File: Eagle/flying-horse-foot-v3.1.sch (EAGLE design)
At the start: 25 parts, among them J2 SPI6, U1 8U2-AU, Y2 16MHz

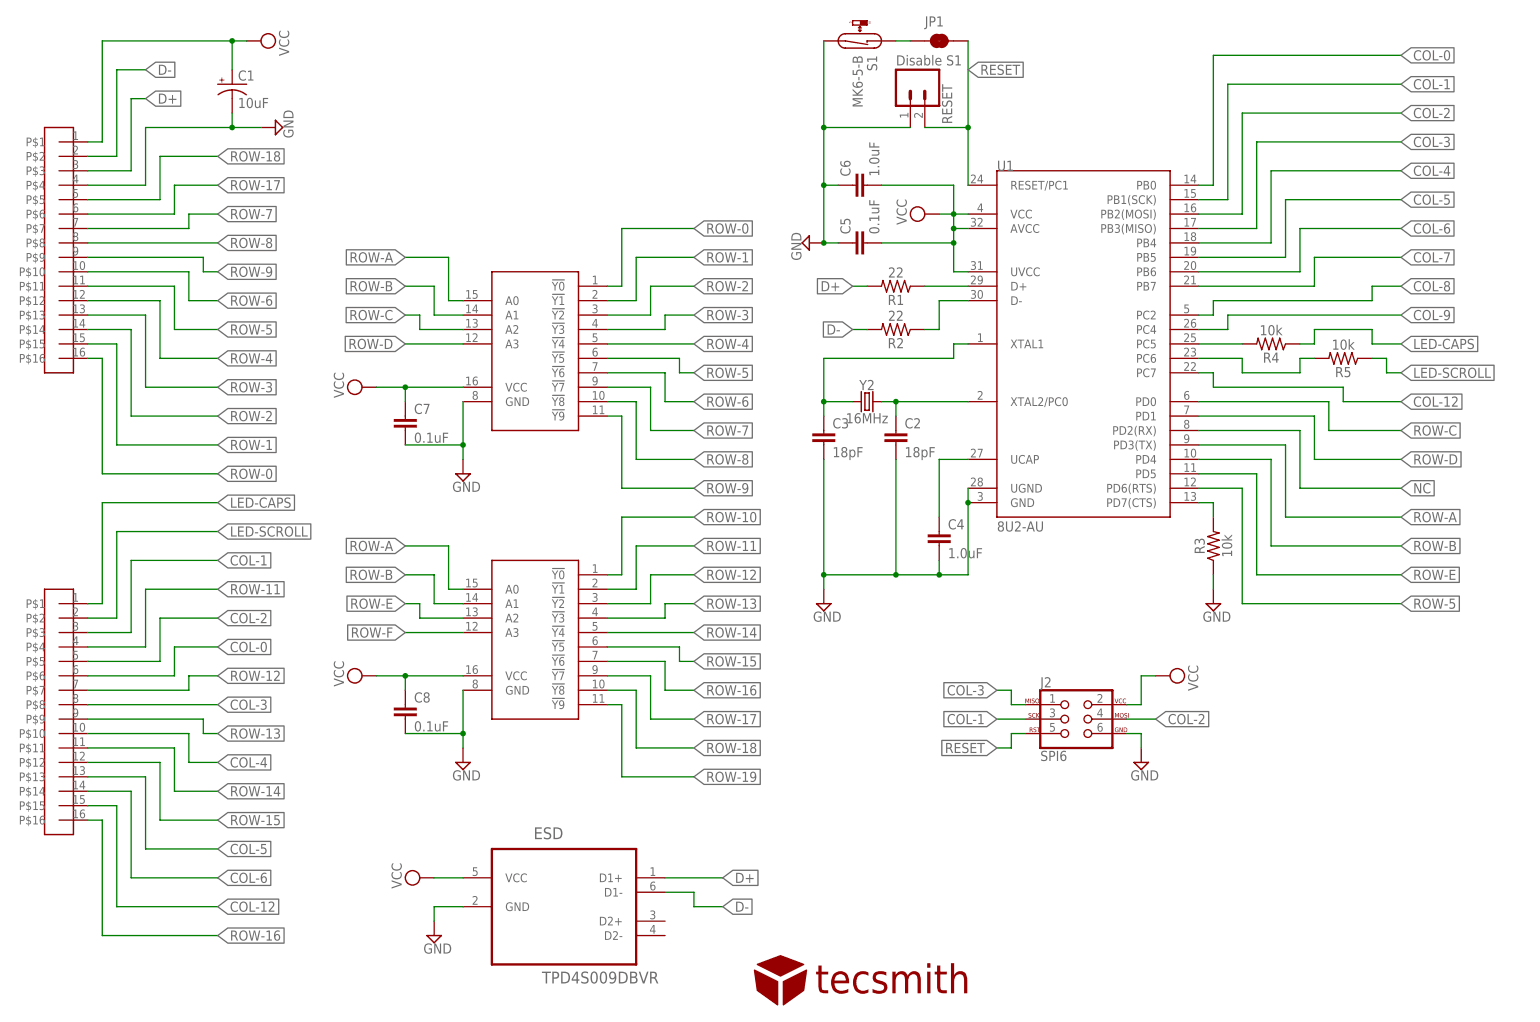
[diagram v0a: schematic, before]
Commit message: moved from 3x2 SPI header to 6x1 SPI header
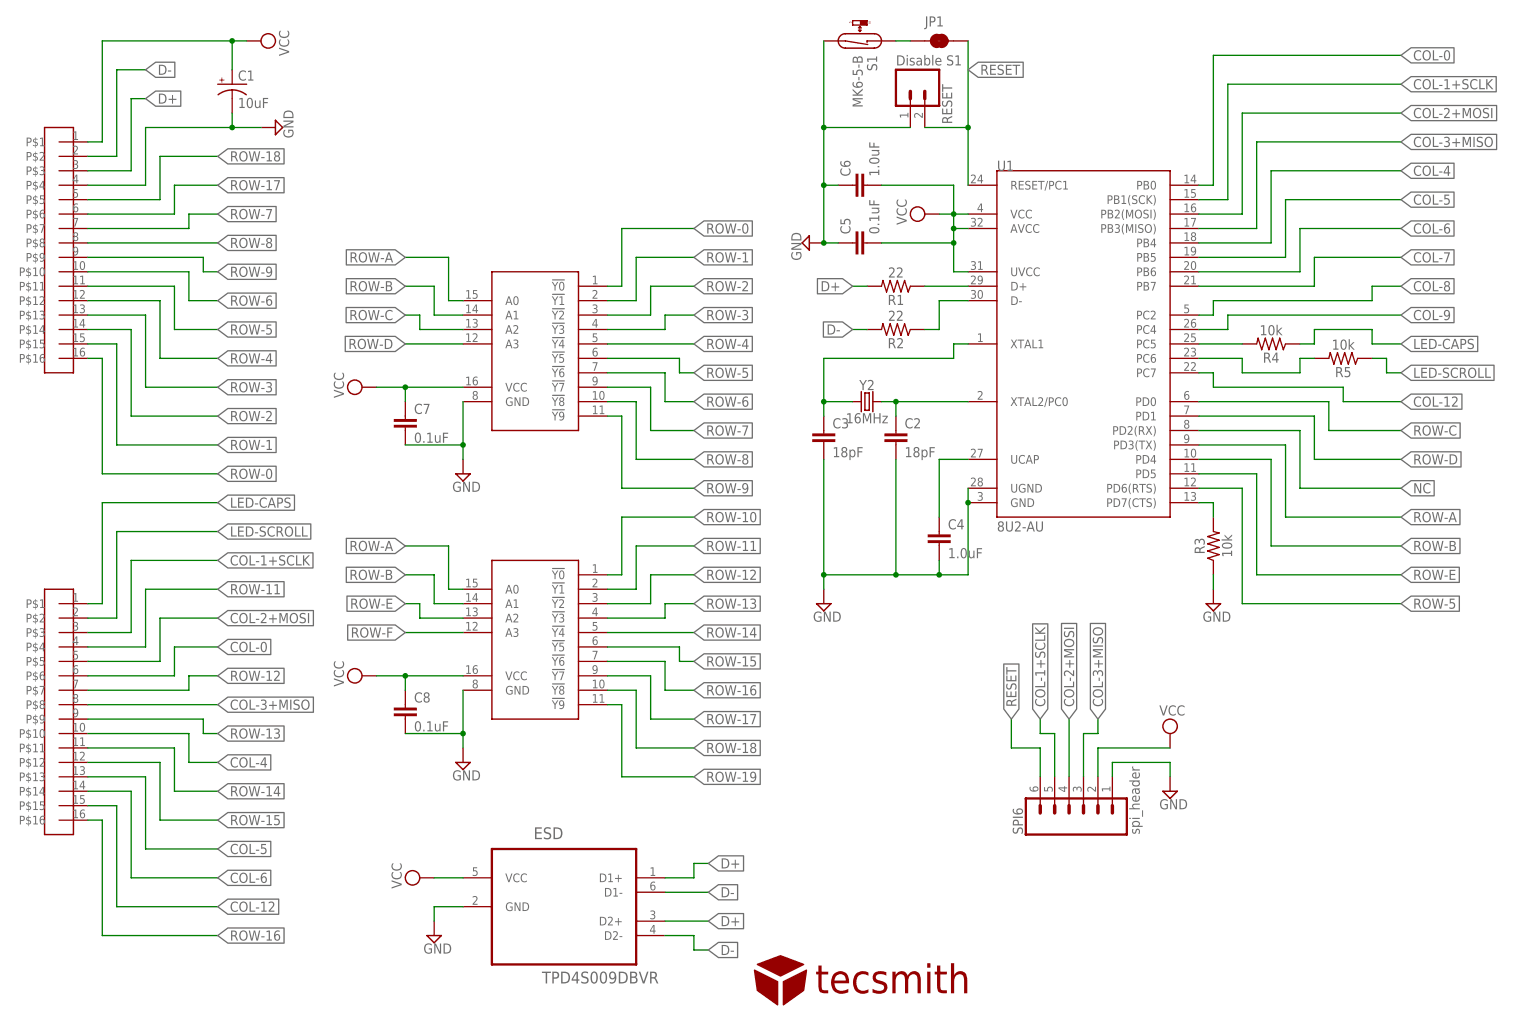
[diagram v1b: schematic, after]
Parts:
- removed J2: SPI6, SparkFun-Connectors:AVR_SPI_PROG_3X2NS
- added SPI6: spi_header, SparkFun-Connectors:CONN_06NO_SILK_NO_POP
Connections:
- removed net COL-1: J2.3, U$4.P$3, U1.PB1(SCK)
- removed net COL-2: J2.4, U$4.P$5, U1.PB2(MOSI)
- removed net COL-3: J2.1, U$4.P$8, U1.PB3(MISO)
- new net COL-1+SCLK: SPI6.5, U$4.P$3, U1.PB1(SCK)
- new net COL-2+MOSI: SPI6.4, U$4.P$5, U1.PB2(MOSI)
- new net COL-3+MISO: SPI6.3, U$4.P$8, U1.PB3(MISO)
- net D+: now also ESD.D2+
- net D-: now also ESD.D2-
- net GND: now also SPI6.1; no longer J2.6
- net RESET: now also SPI6.6; no longer J2.5
- net VCC: now also SPI6.2; no longer J2.2
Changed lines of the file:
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@@
 <part name="SUPPLY11" library="supply2" library_urn="urn:adsk.eagle:library:372" deviceset="VCC" device=""/>
 <part name="SUPPLY12" library="supply2" library_urn="urn:adsk.eagle:library:372" deviceset="VCC" device=""/>
-<part name="J2" library="SparkFun-Connectors" deviceset="AVR_SPI_PROG_3X2" device="NS" value="SPI6"/>
 <part name="JP1" library="SparkFun-Jumpers" deviceset="JUMPER-SMT_2_NC_TRACE" device="_NO-SILK" package3d_urn="urn:adsk.eagle:package:39286/1" value="Disable S1"/>
 <part name="ESD" library="Texas Instruments_By_element14_Batch_1" deviceset="TPD4S009DBVR" device=""/>
@@
 <part name="SUPPLY14" library="supply2" library_urn="urn:adsk.eagle:library:372" deviceset="GND" device=""/>
 <part name="U$5" library="VinoRodrigues_Custom_Eagle" deviceset="TECSMITH-LOGO" device=""/>
+<part name="SPI6" library="SparkFun-Connectors" deviceset="CONN_06" device="NO_SILK_NO_POP" value="spi_header"/>
 </parts>
 <sheets>
@@
 <attribute name="VALUE" x="157.48" y="167.64" size="1.778" layer="96" rot="R270"/>
 </instance>
-<instance part="SUPPLY7" gate="GND" x="208.28" y="43.18" smashed="yes">
-<attribute name="VALUE" x="206.375" y="40.005" size="1.778" layer="96"/>
+<instance part="SUPPLY7" gate="GND" x="213.36" y="38.1" smashed="yes">
+<attribute name="VALUE" x="211.455" y="34.925" size="1.778" layer="96"/>
 </instance>
 <instance part="Y2" gate="G$1" x="160.02" y="106.68" smashed="yes">
@@
 <attribute name="VALUE" x="67.945" y="56.515" size="1.778" layer="96" rot="R90"/>
 </instance>
-<instance part="SUPPLY11" gate="G$1" x="213.36" y="58.42" smashed="yes" rot="R270">
-<attribute name="VALUE" x="216.535" y="60.325" size="1.778" layer="96" rot="R270"/>
+<instance part="SUPPLY11" gate="G$1" x="213.36" y="48.26" smashed="yes">
+<attribute name="VALUE" x="211.455" y="51.435" size="1.778" layer="96"/>
 </instance>
 <instance part="SUPPLY12" gate="G$1" x="53.34" y="170.18" smashed="yes" rot="R270">
 <attribute name="VALUE" x="56.515" y="172.085" size="1.778" layer="96" rot="R270"/>
-</instance>
-<instance part="J2" gate="G$1" x="195.58" y="50.8" smashed="yes">
-<attribute name="NAME" x="190.5" y="56.388" size="1.778" layer="95" font="vector"/>
-<attribute name="VALUE" x="190.5" y="43.434" size="1.778" layer="96" font="vector"/>
 </instance>
 <instance part="JP1" gate="G$1" x="172.72" y="170.18" smashed="yes">
@@
 </instance>
 <instance part="U$5" gate="G$1" x="144.78" y="5.08" smashed="yes"/>
+<instance part="SPI6" gate="G$1" x="198.12" y="35.56" smashed="yes" rot="R90">
+<attribute name="VALUE" x="208.026" y="30.48" size="1.778" layer="96" font="vector" rot="R90"/>
+<attribute name="NAME" x="187.452" y="30.48" size="1.778" layer="95" font="vector" rot="R90"/>
+</instance>
 </instances>
 <busses>
@@
 </segment>
 <segment>
-<label x="134.62" y="17.78" size="1.778" layer="95" xref="yes"/>
+<label x="132.08" y="20.32" size="1.778" layer="95" xref="yes"/>
 <pinref part="ESD" gate="A" pin="D1-"/>
-<wire x1="124.46" y1="20.32" x2="129.54" y2="20.32" width="0.1524" layer="91"/>
-<wire x1="129.54" y1="20.32" x2="129.54" y2="17.78" width="0.1524" layer="91"/>
-<wire x1="129.54" y1="17.78" x2="134.62" y2="17.78" width="0.1524" layer="91"/>
+<wire x1="124.46" y1="20.32" x2="132.08" y2="20.32" width="0.1524" layer="91"/>
+<label x="132.08" y="10.16" size="1.778" layer="95" xref="yes"/>
+</segment>
+<segment>
+<pinref part="ESD" gate="A" pin="D2-"/>
+<wire x1="124.46" y1="12.7" x2="129.54" y2="12.7" width="0.1524" layer="91"/>
+<wire x1="129.54" y1="12.7" x2="129.54" y2="10.16" width="0.1524" layer="91"/>
+<wire x1="129.54" y1="10.16" x2="132.08" y2="10.16" width="0.1524" layer="91"/>
 </segment>
 </net>
@@
 </segment>
 <segment>
-<label x="134.62" y="22.86" size="1.778" layer="95" xref="yes"/>
+<label x="132.08" y="25.4" size="1.778" layer="95" xref="yes"/>
 <pinref part="ESD" gate="A" pin="D1+"/>
-<wire x1="134.62" y1="22.86" x2="124.46" y2="22.86" width="0.1524" layer="91"/>
+<label x="132.08" y="15.24" size="1.778" layer="95" xref="yes"/>
+<wire x1="124.46" y1="22.86" x2="129.54" y2="22.86" width="0.1524" layer="91"/>
+<wire x1="129.54" y1="22.86" x2="129.54" y2="25.4" width="0.1524" layer="91"/>
+<wire x1="129.54" y1="25.4" x2="132.08" y2="25.4" width="0.1524" layer="91"/>
+</segment>
+<segment>
+<pinref part="ESD" gate="A" pin="D2+"/>
+<wire x1="132.08" y1="15.24" x2="124.46" y2="15.24" width="0.1524" layer="91"/>
 </segment>
 </net>
@@
 </segment>
 <segment>
-<wire x1="205.74" y1="48.26" x2="208.28" y2="48.26" width="0.1524" layer="91"/>
 <pinref part="SUPPLY7" gate="GND" pin="GND"/>
-<wire x1="208.28" y1="48.26" x2="208.28" y2="45.72" width="0.1524" layer="91"/>
-<pinref part="J2" gate="G$1" pin="6"/>
+<pinref part="SPI6" gate="G$1" pin="1"/>
+<wire x1="203.2" y1="40.64" x2="203.2" y2="43.18" width="0.1524" layer="91"/>
+<wire x1="203.2" y1="43.18" x2="213.36" y2="43.18" width="0.1524" layer="91"/>
+<wire x1="213.36" y1="43.18" x2="213.36" y2="40.64" width="0.1524" layer="91"/>
 </segment>
 <segment>
@@
 </segment>
 </net>
-<net name="COL-2" class="0">
+<net name="COL-2+MOSI" class="0">
 <segment>
 <pinref part="U1" gate="G$1" pin="PB2(MOSI)"/>
@@
 </segment>
 <segment>
-<wire x1="205.74" y1="50.8" x2="210.82" y2="50.8" width="0.1524" layer="91"/>
-<label x="210.82" y="50.8" size="1.778" layer="95" xref="yes"/>
-<pinref part="J2" gate="G$1" pin="4"/>
+<wire x1="195.58" y1="40.64" x2="195.58" y2="50.8" width="0.1524" layer="91"/>
+<label x="195.58" y="50.8" size="1.778" layer="95" rot="R90" xref="yes"/>
+<pinref part="SPI6" gate="G$1" pin="4"/>
 </segment>
 </net>
@@
 </segment>
 </net>
-<net name="COL-3" class="0">
+<net name="COL-3+MISO" class="0">
 <segment>
 <pinref part="U1" gate="G$1" pin="PB3(MISO)"/>
@@
 </segment>
 <segment>
-<wire x1="187.96" y1="53.34" x2="185.42" y2="53.34" width="0.1524" layer="91"/>
-<wire x1="185.42" y1="53.34" x2="185.42" y2="55.88" width="0.1524" layer="91"/>
-<wire x1="185.42" y1="55.88" x2="182.88" y2="55.88" width="0.1524" layer="91"/>
-<label x="182.88" y="55.88" size="1.778" layer="95" rot="R180" xref="yes"/>
-<pinref part="J2" gate="G$1" pin="1"/>
-</segment>
-</net>
-<net name="COL-1" class="0">
+<label x="200.66" y="50.8" size="1.778" layer="95" rot="R90" xref="yes"/>
+<pinref part="SPI6" gate="G$1" pin="3"/>
+<wire x1="200.66" y1="50.8" x2="200.66" y2="48.26" width="0.1524" layer="91"/>
+<wire x1="200.66" y1="48.26" x2="198.12" y2="48.26" width="0.1524" layer="91"/>
+<wire x1="198.12" y1="48.26" x2="198.12" y2="40.64" width="0.1524" layer="91"/>
+</segment>
+</net>
+<net name="COL-1+SCLK" class="0">
 <segment>
 <pinref part="U1" gate="G$1" pin="PB1(SCK)"/>
@@
 </segment>
 <segment>
-<wire x1="187.96" y1="50.8" x2="182.88" y2="50.8" width="0.1524" layer="91"/>
-<label x="182.88" y="50.8" size="1.778" layer="95" rot="R180" xref="yes"/>
-<pinref part="J2" gate="G$1" pin="3"/>
+<label x="190.5" y="50.8" size="1.778" layer="95" rot="R90" xref="yes"/>
+<pinref part="SPI6" gate="G$1" pin="5"/>
+<wire x1="193.04" y1="40.64" x2="193.04" y2="48.26" width="0.1524" layer="91"/>
+<wire x1="193.04" y1="48.26" x2="190.5" y2="48.26" width="0.1524" layer="91"/>
+<wire x1="190.5" y1="48.26" x2="190.5" y2="50.8" width="0.1524" layer="91"/>
 </segment>
 </net>
@@
 </segment>
 <segment>
-<wire x1="205.74" y1="53.34" x2="208.28" y2="53.34" width="0.1524" layer="91"/>
 <pinref part="SUPPLY11" gate="G$1" pin="VCC"/>
-<wire x1="208.28" y1="53.34" x2="208.28" y2="58.42" width="0.1524" layer="91"/>
-<wire x1="208.28" y1="58.42" x2="210.82" y2="58.42" width="0.1524" layer="91"/>
-<pinref part="J2" gate="G$1" pin="2"/>
+<wire x1="200.66" y1="40.64" x2="200.66" y2="45.72" width="0.1524" layer="91"/>
+<wire x1="200.66" y1="45.72" x2="213.36" y2="45.72" width="0.1524" layer="91"/>
+<pinref part="SPI6" gate="G$1" pin="2"/>
 </segment>
 <segment>
@@
 </segment>
 <segment>
-<wire x1="187.96" y1="48.26" x2="185.42" y2="48.26" width="0.1524" layer="91"/>
-<wire x1="185.42" y1="48.26" x2="185.42" y2="45.72" width="0.1524" layer="91"/>
-<wire x1="185.42" y1="45.72" x2="182.88" y2="45.72" width="0.1524" layer="91"/>
-<label x="182.88" y="45.72" size="1.778" layer="95" rot="R180" xref="yes"/>
-<pinref part="J2" gate="G$1" pin="5"/>
-</segment>
-</net>
+<wire x1="190.5" y1="40.64" x2="190.5" y2="45.72" width="0.1524" layer="91"/>
+<wire x1="190.5" y1="45.72" x2="185.42" y2="45.72" width="0.1524" layer="91"/>
+<wire x1="185.42" y1="45.72" x2="185.42" y2="50.8" width="0.1524" layer="91"/>
+<label x="185.42" y="50.8" size="1.778" layer="95" rot="R90" xref="yes"/>
+<pinref part="SPI6" gate="G$1" pin="6"/>
+</segment>
+</net>

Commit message: second production run, v3.1
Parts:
- added S2: SKRKAEE020, VinoRodrigues_Custom_Eagle:MOMENTARY-SWITCH-SPST-1
- RESET: value (none) -> 0.1 inch 2-pin
- U$1: value 74HC42D16 -> SN74HC42DR
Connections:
- removed net COL-7: U1.PB7
- removed net COL-8: U1.PC2
- removed net COL-9: U1.PC4
- removed net NC: U1.PD2(RX)
- removed net ROW-10: U$2.!Y0
- removed net ROW-19: U$2.!Y9
- net GND: now also S2.1
- net RESET: now also S2.3
- net ROW-5: no longer U1.PD6(RTS)
- net ROW-F: now also U1.PD6(RTS)
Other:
- note added: "3x RESET Options"
- note added: "Optional ESD protection"
- note added: "Optional PCB Switch"
- moved on the sheet: C2, C3, C4, C7, C8, ESD, JP1, RESET, S1, SPI6, Y2

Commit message: typos
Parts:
- ISP6: value spi_header -> isp_header
- renumbered SPI6 to ISP6
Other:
- note added: "ISP Header"
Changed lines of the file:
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@@
 <part name="SUPPLY14" library="supply2" library_urn="urn:adsk.eagle:library:372" deviceset="GND" device=""/>
 <part name="U$5" library="VinoRodrigues_Custom_Eagle" deviceset="TECSMITH-LOGO" device=""/>
-<part name="SPI6" library="SparkFun-Connectors" deviceset="CONN_06" device="NO_SILK_NO_POP" value="spi_header"/>
+<part name="ISP6" library="SparkFun-Connectors" deviceset="CONN_06" device="NO_SILK_NO_POP" value="isp_header"/>
 <part name="S2" library="VinoRodrigues_Custom_Eagle" deviceset="MOMENTARY-SWITCH-SPST-1" device="" value="SKRKAEE020"/>
 <part name="SUPPLY15" library="supply2" library_urn="urn:adsk.eagle:library:372" deviceset="GND" device=""/>
@@
 <text x="208.28" y="58.42" size="1.778" layer="91">Optional ESD protection</text>
 <text x="124.46" y="22.86" size="1.778" layer="91">3x RESET Options</text>
-<text x="101.6" y="15.24" size="1.778" layer="91">Optional PCB Switch</text>
+<text x="101.6" y="12.7" size="1.778" layer="91">Optional PCB Switch</text>
+<text x="165.1" y="25.4" size="1.778" layer="91">ISP Header</text>
 </plain>
 <instances>
@@
 </instance>
 <instance part="U$5" gate="G$1" x="144.78" y="5.08" smashed="yes"/>
-<instance part="SPI6" gate="G$1" x="177.8" y="35.56" smashed="yes" rot="R90">
+<instance part="ISP6" gate="G$1" x="177.8" y="35.56" smashed="yes" rot="R90">
 <attribute name="VALUE" x="187.706" y="30.48" size="1.778" layer="96" font="vector" rot="R90"/>
 <attribute name="NAME" x="167.132" y="30.48" size="1.778" layer="95" font="vector" rot="R90"/>
@@
 <segment>
 <pinref part="SUPPLY7" gate="GND" pin="GND"/>
-<pinref part="SPI6" gate="G$1" pin="1"/>
+<pinref part="ISP6" gate="G$1" pin="1"/>
 <wire x1="182.88" y1="40.64" x2="182.88" y2="43.18" width="0.1524" layer="91"/>
 <wire x1="182.88" y1="43.18" x2="193.04" y2="43.18" width="0.1524" layer="91"/>
@@
 <wire x1="175.26" y1="40.64" x2="175.26" y2="50.8" width="0.1524" layer="91"/>
 <label x="175.26" y="50.8" size="1.778" layer="95" rot="R90" xref="yes"/>
-<pinref part="SPI6" gate="G$1" pin="4"/>
+<pinref part="ISP6" gate="G$1" pin="4"/>
 </segment>
 </net>
@@
 <segment>
 <label x="180.34" y="50.8" size="1.778" layer="95" rot="R90" xref="yes"/>
-<pinref part="SPI6" gate="G$1" pin="3"/>
+<pinref part="ISP6" gate="G$1" pin="3"/>
 <wire x1="180.34" y1="50.8" x2="180.34" y2="48.26" width="0.1524" layer="91"/>
 <wire x1="180.34" y1="48.26" x2="177.8" y2="48.26" width="0.1524" layer="91"/>
@@
 <segment>
 <label x="170.18" y="50.8" size="1.778" layer="95" rot="R90" xref="yes"/>
-<pinref part="SPI6" gate="G$1" pin="5"/>
+<pinref part="ISP6" gate="G$1" pin="5"/>
 <wire x1="172.72" y1="40.64" x2="172.72" y2="48.26" width="0.1524" layer="91"/>
 <wire x1="172.72" y1="48.26" x2="170.18" y2="48.26" width="0.1524" layer="91"/>
@@
 <wire x1="180.34" y1="40.64" x2="180.34" y2="45.72" width="0.1524" layer="91"/>
 <wire x1="180.34" y1="45.72" x2="193.04" y2="45.72" width="0.1524" layer="91"/>
-<pinref part="SPI6" gate="G$1" pin="2"/>
+<pinref part="ISP6" gate="G$1" pin="2"/>
 </segment>
 <segment>
@@
 <wire x1="165.1" y1="45.72" x2="165.1" y2="50.8" width="0.1524" layer="91"/>
 <label x="165.1" y="50.8" size="1.778" layer="95" rot="R90" xref="yes"/>
-<pinref part="SPI6" gate="G$1" pin="6"/>
-</segment>
-<segment>
+<pinref part="ISP6" gate="G$1" pin="6"/>
+</segment>
+<segment>

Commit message: caps and scr led swap
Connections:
- removed net LED-SCROLL: R5.1, U$4.P$2
- new net LED-SCR: R4.1, U$4.P$1
- net LED-CAPS: now also R5.1, U$4.P$2; no longer R4.1, U$4.P$1
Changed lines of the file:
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@@
 </segment>
 </net>
-<net name="LED-CAPS" class="0">
+<net name="LED-SCR" class="0">
 <segment>
 <wire x1="25.4" y1="88.9" x2="45.72" y2="88.9" width="0.1524" layer="91"/>
@@
 </segment>
 </net>
-<net name="LED-SCROLL" class="0">
+<net name="LED-CAPS" class="0">
 <segment>
 <wire x1="22.86" y1="68.58" x2="27.94" y2="68.58" width="0.1524" layer="91"/>

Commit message: ·
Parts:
- S2: device VinoRodrigues_Custom_Eagle:MOMENTARY-SWITCH-SPST-1 -> SilvinoR_Custom_Eagle:MOMENTARY-SWITCH-SPST-1
- U$5: device VinoRodrigues_Custom_Eagle:TECSMITH-LOGO -> SilvinoR_Custom_Eagle:TECSMITH-LOGO
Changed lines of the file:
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@@
 <part name="SUPPLY13" library="supply2" library_urn="urn:adsk.eagle:library:372" deviceset="VCC" device=""/>
 <part name="SUPPLY14" library="supply2" library_urn="urn:adsk.eagle:library:372" deviceset="GND" device=""/>
-<part name="U$5" library="VinoRodrigues_Custom_Eagle" deviceset="TECSMITH-LOGO" device=""/>
+<part name="U$5" library="SilvinoR_Custom_Eagle" deviceset="TECSMITH-LOGO" device=""/>
 <part name="ISP6" library="SparkFun-Connectors" deviceset="CONN_06" device="NO_SILK_NO_POP" value="isp_header"/>
-<part name="S2" library="VinoRodrigues_Custom_Eagle" deviceset="MOMENTARY-SWITCH-SPST-1" device="" value="SKRKAEE020"/>
+<part name="S2" library="SilvinoR_Custom_Eagle" deviceset="MOMENTARY-SWITCH-SPST-1" device="" value="SKRKAEE020"/>
 <part name="SUPPLY15" library="supply2" library_urn="urn:adsk.eagle:library:372" deviceset="GND" device=""/>
 </parts>
